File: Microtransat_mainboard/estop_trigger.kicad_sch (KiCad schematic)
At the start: 5 parts

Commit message: Added regulators and updated GPS, IMU, SD Card symbols
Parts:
- A401: footprint GTMRG_Footprints:Pololu_2802_RCSw -> Microtransat:Pololu RC Switch
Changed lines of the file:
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@@
 			)
 		)
-		(property "Footprint" "GTMRG_Footprints:Pololu_2802_RCSw"
+		(property "Footprint" "Microtransat:Pololu RC Switch"
 			(at 104.14 95.25 0)
 			(effects

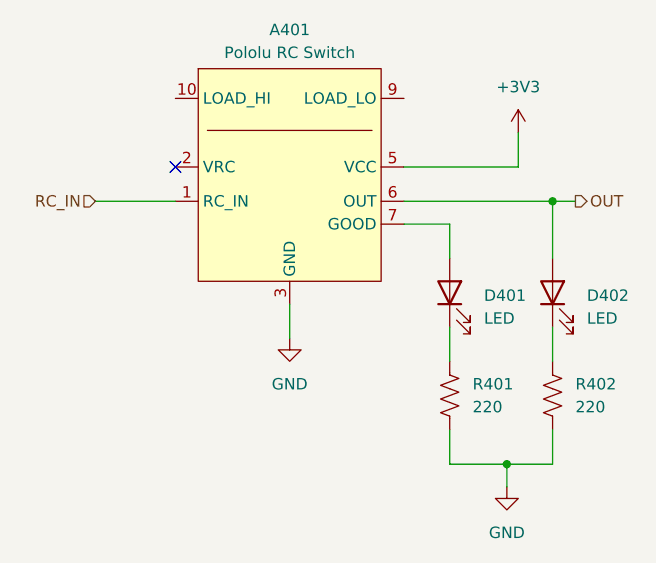
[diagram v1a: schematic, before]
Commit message: Added switch
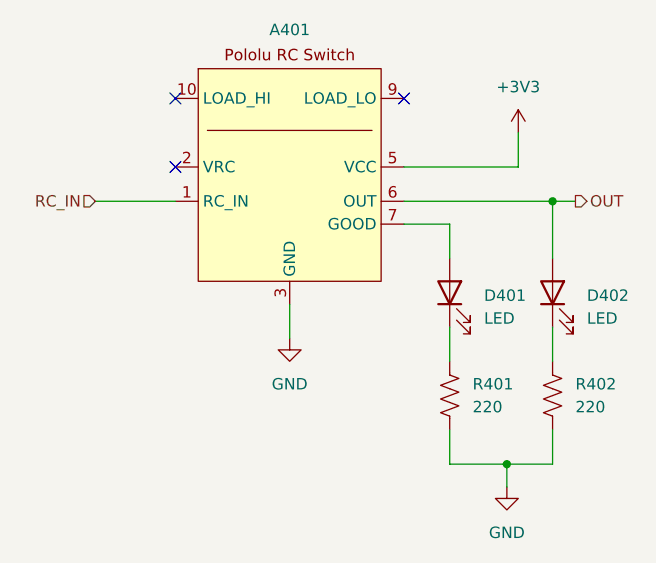
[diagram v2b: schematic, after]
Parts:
- removed A401: Pololu RC Switch, Microtransat:Pololu RC Switch, symbol GTMRG_Boards:Pololu_2802_RCSw
- added A401: ~, Microtransat:Pololu RC Switch, symbol Microtransat:RC_Switch
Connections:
- net +3V3: now also A401.5 (VCC)
- net GND: now also A401.3 (GND), A401.4 (GND), A401.8 (GND)
- net LOAD_HI: now also A401.10 (LOAD_HI), A401.11 (LOAD_HI)
- net OUT: now also A401.6 (OUT)
- net RC_IN: now also A401.1 (RC_IN)
- net at D401.2 (A): now also A401.7 (GOOD)
- no-connect marks 1 -> 3
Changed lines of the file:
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@@
+	)
+	(no_connect
+		(at 116.84 83.82)
 	)
 	(no_connect
 		(at 91.44 91.44)
+	)
+	(no_connect
+		(at 91.44 83.82)
 	)
 	(wire
@@
 			)
 			(justify left)
+		)
+	)
+	(symbol
+		(lib_id "Microtransat:RC_Switch")
+		(at 104.14 91.44 0)
+		(unit 1)
+		(exclude_from_sim no)
+		(in_bom yes)
+		(on_board yes)
+		(dnp no)
+		(fields_autoplaced yes)
+		(property "Reference" "A401"
+			(at 104.14 76.2 0)
+			(effects
+				(font
+					(size 1.27 1.27)
+				)
+			)
+		)
+		(property "Value" "~"
+			(at 104.14 76.2 0)
+			(effects
+				(font
+					(size 1.27 1.27)
+				)
+				(hide yes)
+			)
+		)
+		(property "Footprint" "Microtransat:Pololu RC Switch"
+			(at 104.14 91.44 0)
+			(effects
+				(font
+					(size 1.27 1.27)
+				)
+				(hide yes)
+			)
+		)
+		(property "Datasheet" ""
+			(at 104.14 91.44 0)
+			(effects
+				(font
+					(size 1.27 1.27)
+				)
+				(hide yes)
+			)
+		)
+		(property "Description" ""
+			(at 104.14 91.44 0)
+			(effects
+				(font
+					(size 1.27 1.27)
+				)
+				(hide yes)
+			)
+		)
+		(pin "1"
+		)
+		(pin "9"
+		)
+		(pin "11"
+		)
+		(pin "5"
+		)
+		(pin "10"
+		)
+		(pin "2"
+		)
+		(pin "3"
+		)
+		(pin "4"
+		)
+		(pin "8"
+		)
+		(pin "6"
+		)
+		(pin "7"
+		)
+		(instances
+			(project ""
+				(path "/89914625-be83-416e-bb0d-b792f59b4aa6/b3769bf0-7ef3-4d04-ba3e-5e8a80f01320"
+					(reference "A401")
+					(unit 1)
+				)
+			)
 		)
 	)
@@
 					(unit 1)
 				)
-			)
-		)
-	)
-	(symbol
-		(lib_id "GTMRG_Boards:Pololu_2802_RCSw")
-		(at 104.14 95.25 0)
-		(unit 1)
-		(exclude_from_sim no)
-		(in_bom yes)
-		(on_board yes)
-		(dnp no)
-		(fields_autoplaced yes)
-		(property "Reference" "A401"
-			(at 104.14 76.2 0)
-			(effects
-				(font
-					(size 1.27 1.27)
-				)
-			)
-		)
-		(property "Value" "Pololu RC Switch"
-			(at 104.14 78.74 0)
-			(effects
-				(font
-					(size 1.27 1.27)
-				)
-			)
-		)
-		(property "Footprint" "Microtransat:Pololu RC Switch"
-			(at 104.14 95.25 0)
-			(effects
-				(font
-					(size 1.27 1.27)
-				)
-				(hide yes)
-			)
-		)
-		(property "Datasheet" "https://www.pololu.com/product/2801"
-			(at 104.394 95.25 0)
-			(effects
-				(font
-					(size 1.27 1.27)
-				)
-				(hide yes)
-			)
-		)
-		(property "Description" ""
-			(at 104.14 95.25 0)
-			(effects
-				(font
-					(size 1.27 1.27)
-				)
-				(hide yes)
-			)
-		)
-		(pin "8"
-		)
-		(pin "4"
-		)
-		(pin "3"
-		)
-		(pin "1"
-		)
-		(pin "2"
-		)
-		(pin "11"
-		)
-		(pin "10"
-		)
-		(pin "7"
-		)
-		(pin "5"
-		)
-		(pin "9"
-		)
-		(pin "6"
-		)
-		(instances
-			(project "Microtransat_mainboard"
-				(path "/89914625-be83-416e-bb0d-b792f59b4aa6/b3769bf0-7ef3-4d04-ba3e-5e8a80f01320"
-					(reference "A401")
-					(unit 1)
-				)
